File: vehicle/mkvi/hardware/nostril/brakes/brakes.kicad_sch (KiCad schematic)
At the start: 0 parts

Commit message: updates from LV design check
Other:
- sheet Power ports: added +BATT; removed none
- sheet Shutdown Sense ports: added BSPD_LL; removed BSPD_LL_OUT
- note added: "Analog Brakelight output circuitry - toggles brakelight based on brake pressure"
- note added: "Buck converter downregulates +12V to +5v @ max 500mA"
- note added: "CAN, Status LEDS, microcontroller, programming pins"
- note added: "Driver for upstream modeule-by-module fault detection"
- note added: "Logic + timer circuit to control BSPD Shutdown state"
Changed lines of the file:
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@@
+    (stroke (width 0) (type default) (color 0 0 0 0))
+  )
+  (wire (pts (xy 155.829 52.832) (xy 160.02 52.832))
     (stroke (width 0) (type default) (color 0 0 0 0))
   )
@@
   (wire (pts (xy 199.39 127) (xy 231.14 127))
     (stroke (width 0) (type default) (color 0 0 0 0))
+  )
+  (text "Buck converter downregulates\n+12V to +5v @ max 500mA"
+    (at 311.15 54.102 0)
+    (effects (font (size 1.27 1.27)) (justify left bottom))
+  )
+  (text "Logic + timer circuit to\ncontrol BSPD Shutdown state"
+    (at 310.261 127.889 0)
+    (effects (font (size 1.27 1.27)) (justify left bottom))
+  )
+  (text "Analog Brakelight output\ncircuitry - toggles brakelight\nbased on brake pressure"
+    (at 311.404 90.17 0)
+    (effects (font (size 1.27 1.27)) (justify left bottom))
+  )
+  (text "Driver for upstream\nmodeule-by-module fault \ndetection"
+    (at 286.639 161.798 0)
+    (effects (font (size 1.27 1.27)) (justify left bottom))
+  )
+  (text "CAN, Status LEDS,\nmicrocontroller,\nprogramming pins"
+    (at 158.877 108.331 0)
+    (effects (font (size 1.27 1.27)) (justify right bottom))
+  )
+  (global_label "V_BATT" (shape input) (at 155.829 52.832 90) (fields_autoplaced)
+    (effects (font (size 1.27 1.27)) (justify left))
+    (property "Intersheet References" "${INTERSHEET_REFS}" (id 0) (at 155.9084 44.1578 90)
+      (effects (font (size 1.27 1.27)) (justify left) hide)
+    )
   )
   (sheet (at 160.02 71.12) (size 39.37 71.12) (fields_autoplaced)
@@
       (effects (font (size 1.27 1.27)) (justify left top))
     )
+    (pin "+BATT" input (at 160.02 52.832 180)
+      (effects (font (size 1.27 1.27)) (justify left))
+    )
   )
   (sheet (at 255.27 71.12) (size 54.61 31.75) (fields_autoplaced)
@@
       (effects (font (size 1.27 1.27)) (justify left top))
     )
-    (pin "BSPD_LL_OUT" input (at 255.27 156.21 180)
+    (pin "BSPD_LL" input (at 255.27 156.21 180)
       (effects (font (size 1.27 1.27)) (justify left))
     )
@@
     )
   )
-  (sheet (at 191.77 173.99) (size 71.12 26.67) (fields_autoplaced)
+  (sheet (at 185.8518 173.99) (size 77.0382 26.1366)
     (stroke (width 0.1524) (type solid) (color 0 0 0 0))
     (fill (color 0 0 0 0.0000))
-    (property "Sheet name" "M.2 Connector" (id 0) (at 191.0584 200.66 90)
+    (property "Sheet name" "M.2 Connector" (id 0) (at 185.8518 173.3296 0)
       (effects (font (size 1.27 1.27)) (justify left bottom))
     )
-    (property "Sheet file" "Connector.kicad_sch" (id 1) (at 263.4746 200.66 90)
+    (property "Sheet file" "Connector.kicad_sch" (id 1) (at 185.8518 201.3204 0)
       (effects (font (size 1.27 1.27)) (justify left top))
     )
@@
       (reference "#PWR?") (unit 1) (value "GND") (footprint "")
     )
-    (path "/185b9e35-936e-4231-b044-c2356c1f5f5e/d45a5b6e-6862-4c98-8ce0-88025572e7cb"
-      (reference "#PWR?") (unit 1) (value "+BATT") (footprint "")
-    )
     (path "/185b9e35-936e-4231-b044-c2356c1f5f5e/65087877-5d0d-4e11-9297-9cfa67fb9169"
       (reference "#PWR?") (unit 1) (value "GND") (footprint "")
@@
       (reference "#PWR?") (unit 1) (value "GND") (footprint "")
     )
-    (path "/718fe271-d81c-4ddf-8baf-ccfb6ae290e3/7a1ef4d7-9c90-40ba-b6ae-c305632a144f"
-      (reference "#PWR?") (unit 1) (value "+BATT") (footprint "")
-    )
     (path "/063f9baa-9e7f-4e30-8189-9b7cdc546808/9537f014-8338-4794-972d-42d8e54f702f"
       (reference "#PWR?") (unit 1) (value "GND") (footprint "")
@@
       (reference "D1") (unit 1) (value "BSPD_GATE_TRIP") (footprint "footprints:LED_0805_OEM")
     )
-    (path "/e279e344-9058-4851-bdde-ca605e652c75/50124339-49ac-4499-9ca0-4f55703537d9"
-      (reference "D2") (unit 1) (value "Diode_600V_1A_SM") (footprint "footprints:Diode_600V_1A_SM")
+    (path "/e279e344-9058-4851-bdde-ca605e652c75/3c1c5502-98f9-4a36-bdc3-0984dc10ac80"
+      (reference "D2") (unit 1) (value "D_Zener_18V") (footprint "footprints:DO-214AA")
     )
     (path "/e279e344-9058-4851-bdde-ca605e652c75/9a0bfd90-3ac1-4a4a-816a-053629045328"
@@
       (reference "D10") (unit 1) (value "Shutdown_LED") (footprint "footprints:LED_0805_OEM")
     )
+    (path "/063f9baa-9e7f-4e30-8189-9b7cdc546808/73c1f970-e896-4a19-8d33-45ba269222b6"
+      (reference "D11") (unit 1) (value "MISO_PROG_LED") (footprint "footprints:LED_0805_OEM")
+    )
     (path "/063f9baa-9e7f-4e30-8189-9b7cdc546808/0998b122-48e6-475b-8840-b9517e6eb4ce"
-      (reference "D?") (unit 1) (value "MOSI_PROG_LED") (footprint "footprints:LED_0805_OEM")
-    )
-    (path "/063f9baa-9e7f-4e30-8189-9b7cdc546808/73c1f970-e896-4a19-8d33-45ba269222b6"
-      (reference "D?") (unit 1) (value "MISO_PROG_LED") (footprint "footprints:LED_0805_OEM")
+      (reference "D12") (unit 1) (value "MOSI_PROG_LED") (footprint "footprints:LED_0805_OEM")
     )
     (path "/185b9e35-936e-4231-b044-c2356c1f5f5e/188c9ed8-cc0a-4815-8ae7-63298e8f61e8"
@@
       (reference "R32") (unit 1) (value "R_10K") (footprint "footprints:R_0805_OEM")
     )
+    (path "/063f9baa-9e7f-4e30-8189-9b7cdc546808/ff97ae9f-bbf0-4529-9240-769c48934eaf"
+      (reference "R33") (unit 1) (value "R_200") (footprint "footprints:R_0805_OEM")
+    )
     (path "/063f9baa-9e7f-4e30-8189-9b7cdc546808/c17afb13-5c5c-49fa-bd34-544c7f61c97b"
-      (reference "R?") (unit 1) (value "R_200") (footprint "footprints:R_0805_OEM")
-    )
-    (path "/063f9baa-9e7f-4e30-8189-9b7cdc546808/ff97ae9f-bbf0-4529-9240-769c48934eaf"
-      (reference "R?") (unit 1) (value "R_200") (footprint "footprints:R_0805_OEM")
+      (reference "R34") (unit 1) (value "R_200") (footprint "footprints:R_0805_OEM")
     )
     (path "/e279e344-9058-4851-bdde-ca605e652c75/9608e81f-cbe0-462b-8a9a-2b8ab6c02948"

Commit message: got rid of extra files
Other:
- removed sheet Power
- note removed: "Buck converter downregulates +12V to +5v @ max 500mA"

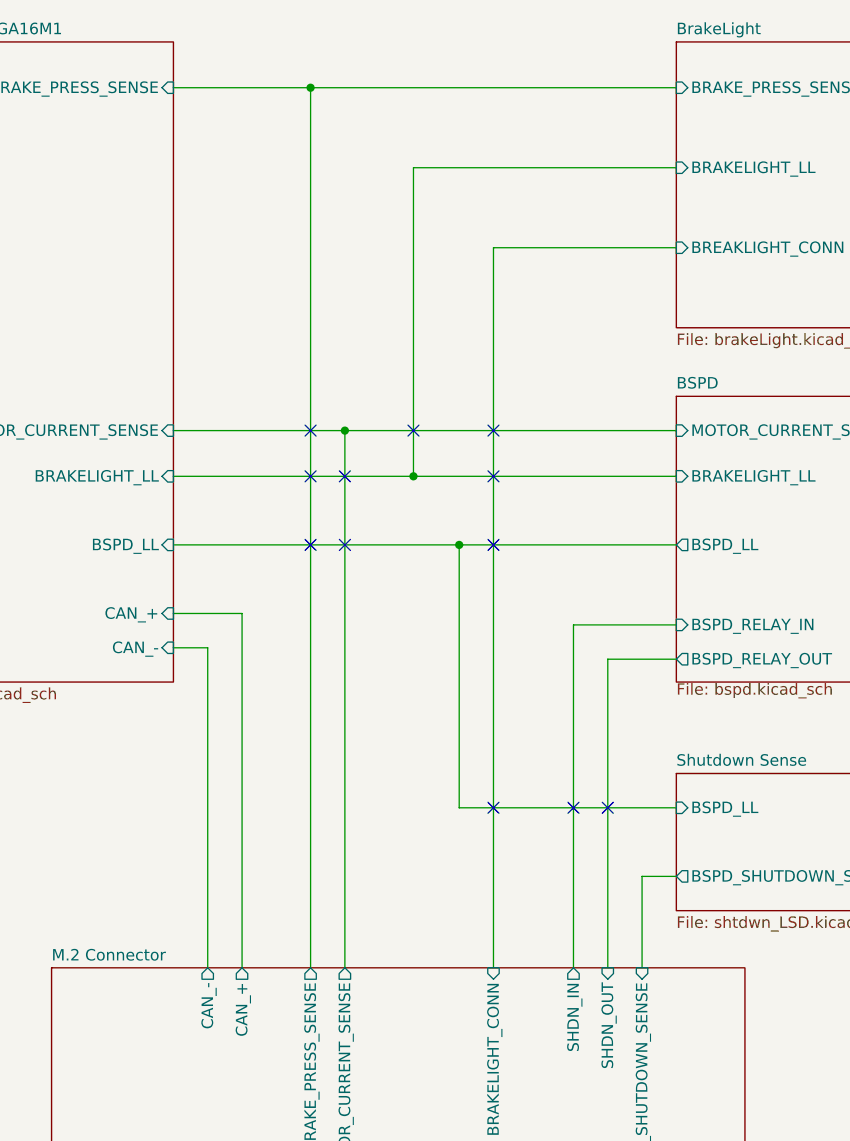
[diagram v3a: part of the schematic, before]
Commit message: BSPD PCB Update (#204)
* first draft of schematic

* Updated Brakes Board

* Revised a bit of the brakes board

* try 2

* updates from LV design check

* edit BUILD file to add heirarchical (eek spelling?) files

* response schematic after reviews

* BUILD file update

* fix bazel build

* got rid of extra files

* added PCB board layout and updated schematic

* added some coolish silkscreen stuff and responded to jack's comments

* forgot board name

* added seperate buttons for brakelight and 5kW overrides

* ground plane plus bypass pins

* silkscreen logo

* Revert changes to precharge/discharge

Co-authored-by: Ian <iwalsh@olin.edu>
Co-authored-by: Jack Greenberg <j@jackgreenberg.co>
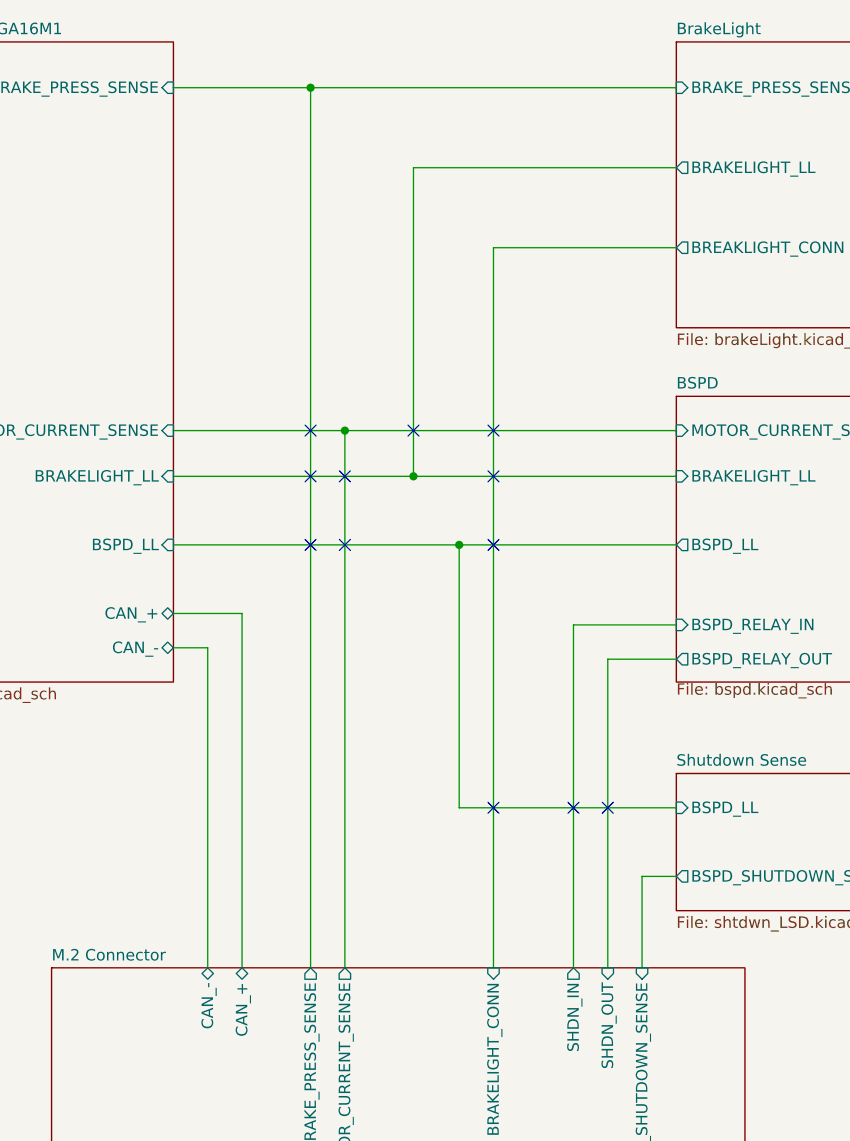
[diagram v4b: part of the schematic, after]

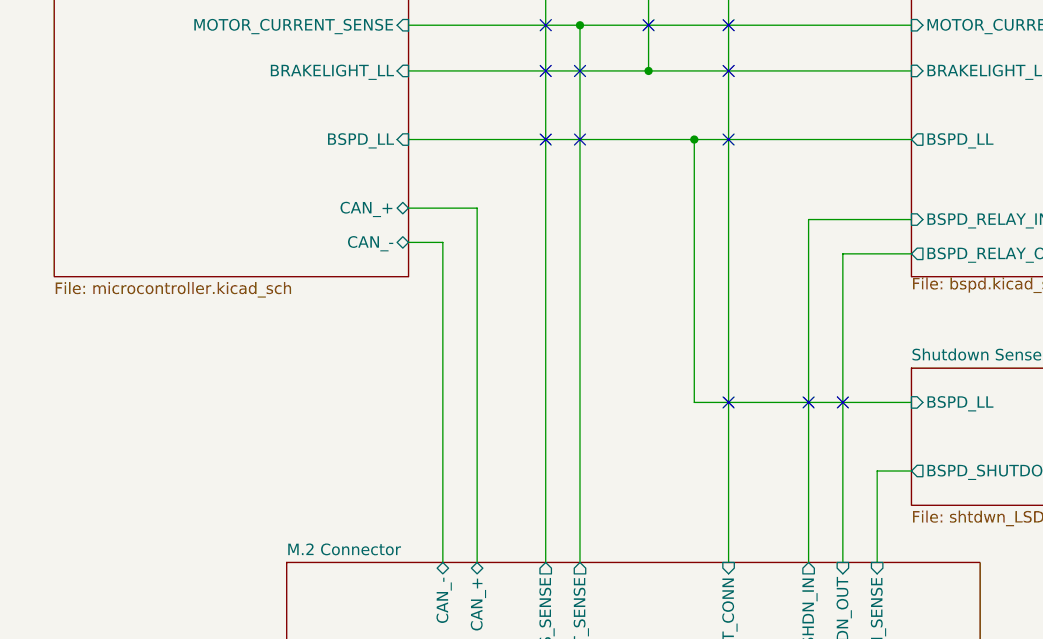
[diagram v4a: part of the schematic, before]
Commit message: add bspd SS to microcontroller (#210)
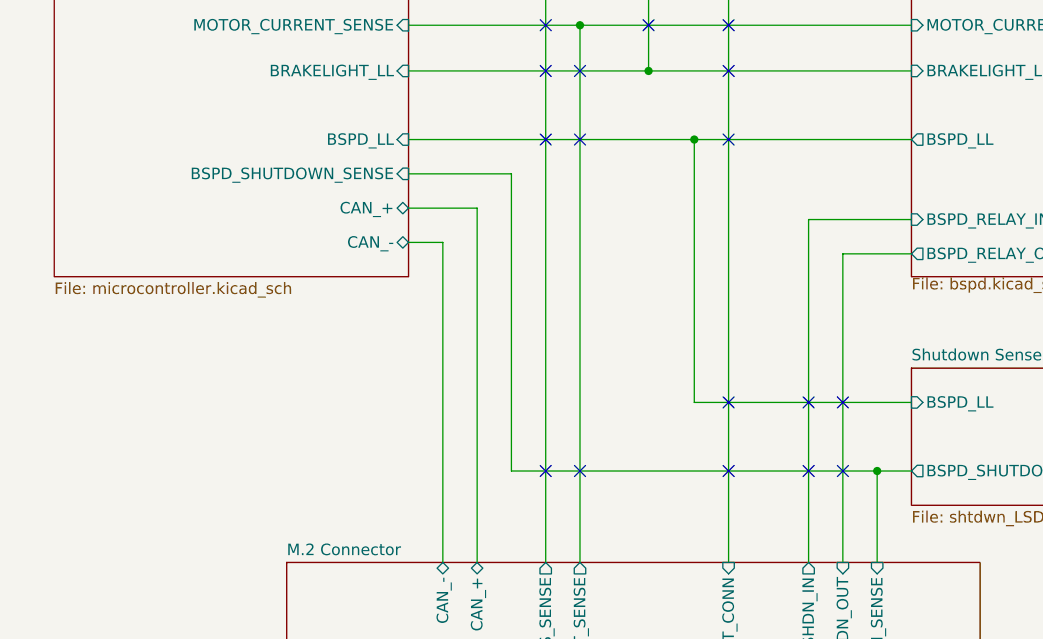
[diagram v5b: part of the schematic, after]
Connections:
- no-connect marks 12 -> 17
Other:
- sheet Microcontroller - ATMEGA16M1 ports: added BSPD_SHUTDOWN_SENSE; removed none
